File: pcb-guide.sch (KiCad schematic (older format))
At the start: 14 parts

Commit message: Tags added
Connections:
- net labels added: D+, D-
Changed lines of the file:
@@
 Wire Wire Line
 	2250 1400 2350 1400
+Text GLabel 1550 2400 0    50   Input ~ 0
+D+
+Text GLabel 1550 2500 0    50   Input ~ 0
+D-
 $EndSCHEMATC

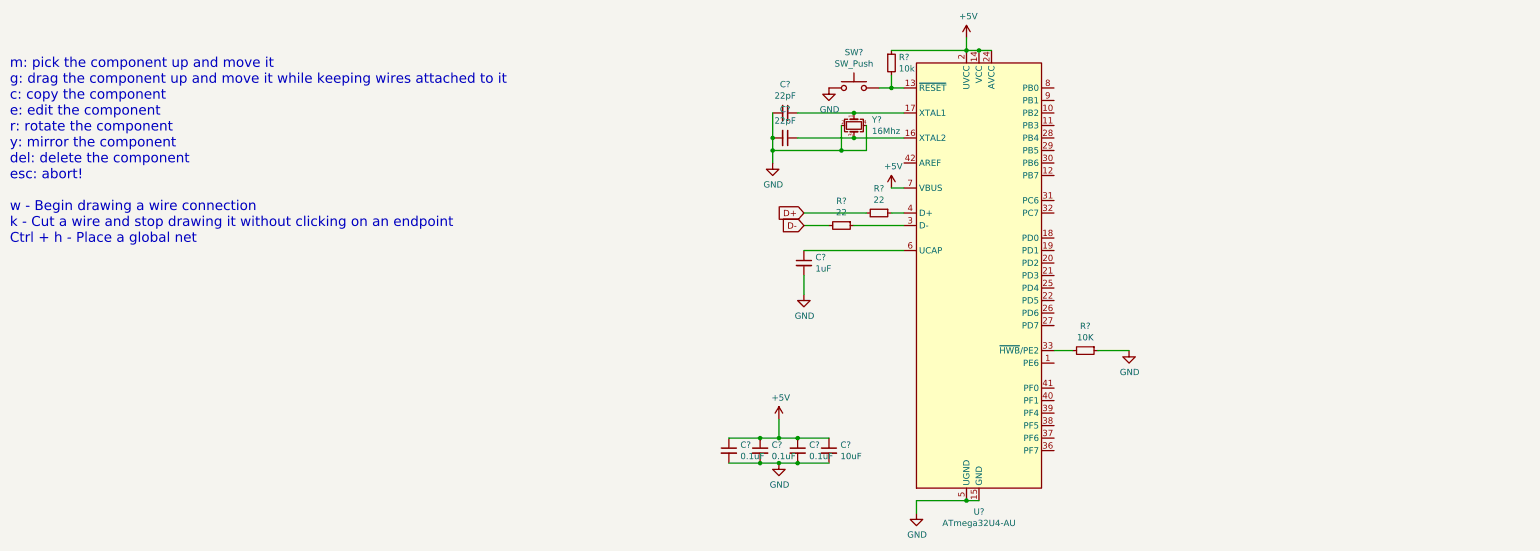
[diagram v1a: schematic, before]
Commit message: part4 finished mx_alps_hybrid not found in footpritn libraries
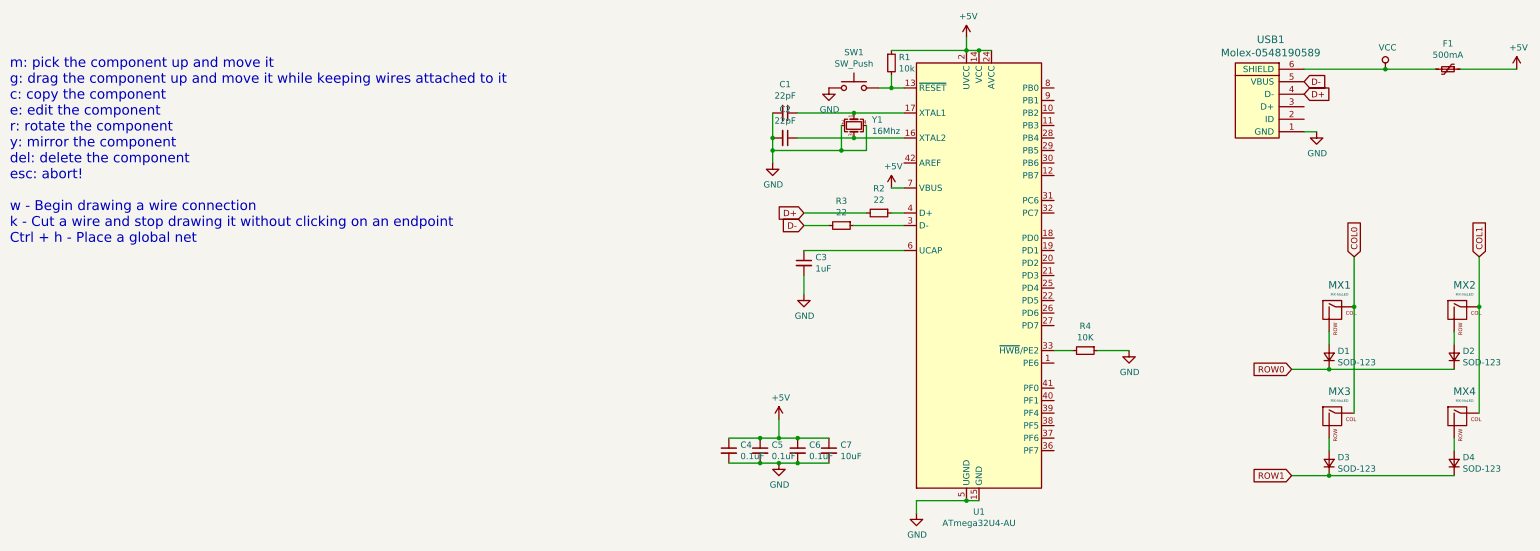
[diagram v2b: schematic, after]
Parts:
- added D1, D2, D3, D4: SOD-123, Diode_SMD:D_SOD-123, symbol Device:D_Small
- added F1: 500mA, Fuse:Fuse_1206_3216Metric, symbol Device:Polyfuse_Small
- added MX1, MX2, MX3, MX4: MX-NoLED, symbol MX_Alps_Hybrid:MX-NoLED
- added USB1: Molex-0548190589, random-keyboard-parts:Molex-0548190589, symbol random-keyboard-parts:Molex-0548190589
- C1, C2, C3, C4, C5, C6, C7: renamed from C?; footprint (none) -> Capacitor_SMD:C_0805_2012Metric
- R1, R2, R3, R4: renamed from R?; footprint (none) -> Resistor_SMD:R_0805_2012Metric
- SW1: renamed from SW?; footprint (none) -> random-keyboard-parts:SKQG-1155865
- Y1: renamed from Y?; footprint (none) -> Crystal:Crystal_SMD_3225-4Pin_3.2x2.5mm
- gave numbers to parts that had none: 1
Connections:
- net +5V: now also F1.1
- net D+: now also USB1.4 (D-)
- net D-: now also USB1.5 (VBUS)
- net GND: now also USB1.1 (GND)
- new net: D1.2 (A), MX1.2 (ROW)
- new net: D2.2 (A), MX2.2 (ROW)
- new net: D3.2 (A), MX3.2 (ROW)
- new net: D4.2 (A), MX4.2 (ROW)
- new net COL0: MX1.1 (COL), MX3.1 (COL)
- new net COL1: MX2.1 (COL), MX4.1 (COL)
- new net ROW0: D1.1 (K), D2.1 (K)
- new net ROW1: D3.1 (K), D4.1 (K)
- new net VCC: F1.2, USB1.6 (SHIELD)

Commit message: Error fixed with MX_ALPS_Hybrid
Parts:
- MX1, MX2, MX3, MX4: footprint (none) -> MX_Alps_Hybrid:MX-1U-NoLED
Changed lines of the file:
@@
 F 0 "MX1" H 5833 3423 60  0000 C CNN
 F 1 "MX-NoLED" H 5833 3349 20  0000 C CNN
-F 2 "" H 5175 3175 60  0001 C CNN
+F 2 "MX_Alps_Hybrid:MX-1U-NoLED" H 5175 3175 60  0001 C CNN
 F 3 "" H 5175 3175 60  0001 C CNN
 	1    5800 3200
@@
 F 0 "MX2" H 6833 3423 60  0000 C CNN
 F 1 "MX-NoLED" H 6833 3349 20  0000 C CNN
-F 2 "" H 6175 3175 60  0001 C CNN
+F 2 "MX_Alps_Hybrid:MX-1U-NoLED" H 6175 3175 60  0001 C CNN
 F 3 "" H 6175 3175 60  0001 C CNN
 	1    6800 3200
@@
 F 0 "MX3" H 5833 4273 60  0000 C CNN
 F 1 "MX-NoLED" H 5833 4199 20  0000 C CNN
-F 2 "" H 5175 4025 60  0001 C CNN
+F 2 "MX_Alps_Hybrid:MX-1U-NoLED" H 5175 4025 60  0001 C CNN
 F 3 "" H 5175 4025 60  0001 C CNN
 	1    5800 4050
@@
 F 0 "MX4" H 6833 4273 60  0000 C CNN
 F 1 "MX-NoLED" H 6833 4199 20  0000 C CNN
-F 2 "" H 6175 4025 60  0001 C CNN
+F 2 "MX_Alps_Hybrid:MX-1U-NoLED" H 6175 4025 60  0001 C CNN
 F 3 "" H 6175 4025 60  0001 C CNN
 	1    6800 4050

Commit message: part 5 almost finished
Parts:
- MX1, MX2, MX3, MX4: footprint MX_Alps_Hybrid:MX-1U-NoLED -> MX_Alps_Hybrid:MX-1U
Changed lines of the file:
@@
 F 0 "MX1" H 5833 3423 60  0000 C CNN
 F 1 "MX-NoLED" H 5833 3349 20  0000 C CNN
-F 2 "MX_Alps_Hybrid:MX-1U-NoLED" H 5175 3175 60  0001 C CNN
+F 2 "MX_Alps_Hybrid:MX-1U" H 5175 3175 60  0001 C CNN
 F 3 "" H 5175 3175 60  0001 C CNN
 	1    5800 3200
@@
 F 0 "MX2" H 6833 3423 60  0000 C CNN
 F 1 "MX-NoLED" H 6833 3349 20  0000 C CNN
-F 2 "MX_Alps_Hybrid:MX-1U-NoLED" H 6175 3175 60  0001 C CNN
+F 2 "MX_Alps_Hybrid:MX-1U" H 6175 3175 60  0001 C CNN
 F 3 "" H 6175 3175 60  0001 C CNN
 	1    6800 3200
@@
 F 0 "MX3" H 5833 4273 60  0000 C CNN
 F 1 "MX-NoLED" H 5833 4199 20  0000 C CNN
-F 2 "MX_Alps_Hybrid:MX-1U-NoLED" H 5175 4025 60  0001 C CNN
+F 2 "MX_Alps_Hybrid:MX-1U" H 5175 4025 60  0001 C CNN
 F 3 "" H 5175 4025 60  0001 C CNN
 	1    5800 4050
@@
 F 0 "MX4" H 6833 4273 60  0000 C CNN
 F 1 "MX-NoLED" H 6833 4199 20  0000 C CNN
-F 2 "MX_Alps_Hybrid:MX-1U-NoLED" H 6175 4025 60  0001 C CNN
+F 2 "MX_Alps_Hybrid:MX-1U" H 6175 4025 60  0001 C CNN
 F 3 "" H 6175 4025 60  0001 C CNN
 	1    6800 4050

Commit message: Finish
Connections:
- net COL0: now also U1.29 (PB5)
- net COL1: now also U1.28 (PB4)
- net ROW0: now also U1.27 (PD7)
- net ROW1: now also U1.30 (PB6)
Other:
- moved on the sheet: R4
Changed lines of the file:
@@
 L power:GND #PWR0103
 U 1 1 5FBEA79A
-P 4150 3500
-F 0 "#PWR0103" H 4150 3250 50  0001 C CNN
-F 1 "GND" H 4155 3327 50  0000 C CNN
-F 2 "" H 4150 3500 50  0001 C CNN
-F 3 "" H 4150 3500 50  0001 C CNN
-	1    4150 3500
+P 4400 3500
+F 0 "#PWR0103" H 4400 3250 50  0001 C CNN
+F 1 "GND" H 4405 3327 50  0000 C CNN
+F 2 "" H 4400 3500 50  0001 C CNN
+F 3 "" H 4400 3500 50  0001 C CNN
+	1    4400 3500
 	1    0    0    -1
 $EndComp
@@
 L Device:R_Small R4
 U 1 1 5FBEB9A0
-P 3800 3500
-F 0 "R4" V 3604 3500 50  0000 C CNN
-F 1 "10K" V 3695 3500 50  0000 C CNN
-F 2 "Resistor_SMD:R_0805_2012Metric" H 3800 3500 50  0001 C CNN
-F 3 "~" H 3800 3500 50  0001 C CNN
-	1    3800 3500
-	0    1    1    0
-$EndComp
-Wire Wire Line
-	3550 3500 3700 3500
-Wire Wire Line
-	3900 3500 4150 3500
+P 4050 3500
+F 0 "R4" V 3854 3500 50  0000 C CNN
+F 1 "10K" V 3945 3500 50  0000 C CNN
+F 2 "Resistor_SMD:R_0805_2012Metric" H 4050 3500 50  0001 C CNN
+F 3 "~" H 4050 3500 50  0001 C CNN
+	1    4050 3500
+	0    1    1    0
+$EndComp
+Wire Wire Line
+	4150 3500 4400 3500
 $Comp
 L Device:R_Small R2
@@
 Text GLabel 6950 2750 1    50   Input ~ 0
 COL1
+Text GLabel 3550 1800 2    50   Input ~ 0
+COL1
+Text GLabel 3550 1900 2    50   Input ~ 0
+COL0
+Text GLabel 3550 2000 2    50   Input ~ 0
+ROW1
+Text GLabel 3550 3300 2    50   Input ~ 0
+ROW0
+Wire Wire Line
+	3950 3500 3550 3500
 $EndSCHEMATC

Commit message: PCB finished
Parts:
- MX1, MX2, MX3, MX4: footprint MX_Alps_Hybrid:MX-1U -> MX_Only:MXOnly-1U
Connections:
- net D+: now also USB1.3 (D+); no longer USB1.4 (D-)
- net D-: now also USB1.4 (D-); no longer USB1.5 (VBUS)
- net VCC: now also USB1.5 (VBUS); no longer USB1.6 (SHIELD)
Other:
- moved on the sheet: F1, USB1
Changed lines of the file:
@@
 $EndComp
-Wire Wire Line
-	2950 4700 2850 4700
 Wire Wire Line
 	2850 4700 2450 4700
 Wire Wire Line
 	2450 4700 2450 4800
-Connection ~ 2850 4700
 $Comp
 L power:GND #PWR0103
@@
 L random-keyboard-parts:Molex-0548190589 USB1
 U 1 1 5FC20C0B
-P 5250 1550
-F 0 "USB1" V 5787 1517 60  0000 C CNN
-F 1 "Molex-0548190589" V 5681 1517 60  0000 C CNN
-F 2 "random-keyboard-parts:Molex-0548190589" H 5250 1550 60  0001 C CNN
-F 3 "" H 5250 1550 60  0001 C CNN
-	1    5250 1550
+P 5100 1550
+F 0 "USB1" V 5637 1517 60  0000 C CNN
+F 1 "Molex-0548190589" V 5531 1517 60  0000 C CNN
+F 2 "random-keyboard-parts:Molex-0548190589" H 5100 1550 60  0001 C CNN
+F 3 "" H 5100 1550 60  0001 C CNN
+	1    5100 1550
 	0    -1   -1   0
 $EndComp
-$Comp
-L power:VCC #PWR0110
-U 1 1 5FC21D9D
-P 6200 1250
-F 0 "#PWR0110" H 6200 1100 50  0001 C CNN
-F 1 "VCC" H 6217 1423 50  0000 C CNN
-F 2 "" H 6200 1250 50  0001 C CNN
-F 3 "" H 6200 1250 50  0001 C CNN
-	1    6200 1250
-	1    0    0    -1
-$EndComp
-$Comp
-L Device:Polyfuse_Small F1
-U 1 1 5FC22CD6
-P 6700 1250
-F 0 "F1" V 6495 1250 50  0000 C CNN
-F 1 "500mA" V 6586 1250 50  0000 C CNN
-F 2 "Fuse:Fuse_1206_3216Metric" H 6750 1050 50  0001 L CNN
-F 3 "~" H 6700 1250 50  0001 C CNN
-	1    6700 1250
-	0    1    1    0
-$EndComp
-$Comp
-L power:+5V #PWR0111
-U 1 1 5FC23944
-P 7250 1250
-F 0 "#PWR0111" H 7250 1100 50  0001 C CNN
-F 1 "+5V" H 7265 1423 50  0000 C CNN
-F 2 "" H 7250 1250 50  0001 C CNN
-F 3 "" H 7250 1250 50  0001 C CNN
-	1    7250 1250
-	1    0    0    -1
-$EndComp
-Wire Wire Line
-	5550 1250 6200 1250
-Wire Wire Line
-	6600 1250 6200 1250
-Connection ~ 6200 1250
-Wire Wire Line
-	6800 1250 7250 1250
-Text GLabel 5550 1450 2    50   Input ~ 0
+Text GLabel 5400 1550 2    50   Input ~ 0
 D+
-Text GLabel 5550 1350 2    50   Input ~ 0
+Text GLabel 5400 1450 2    50   Input ~ 0
 D-
 $Comp
 L power:GND #PWR0112
 U 1 1 5FC2A78A
-P 5650 1750
-F 0 "#PWR0112" H 5650 1500 50  0001 C CNN
-F 1 "GND" H 5655 1577 50  0000 C CNN
-F 2 "" H 5650 1750 50  0001 C CNN
-F 3 "" H 5650 1750 50  0001 C CNN
-	1    5650 1750
-	1    0    0    -1
-$EndComp
-Wire Wire Line
-	5550 1750 5650 1750
+P 5500 1750
+F 0 "#PWR0112" H 5500 1500 50  0001 C CNN
+F 1 "GND" H 5505 1577 50  0000 C CNN
+F 2 "" H 5500 1750 50  0001 C CNN
+F 3 "" H 5500 1750 50  0001 C CNN
+	1    5500 1750
+	1    0    0    -1
+$EndComp
+Wire Wire Line
+	5400 1750 5500 1750
 $Comp
 L MX_Alps_Hybrid:MX-NoLED MX1
@@
 F 0 "MX1" H 5833 3423 60  0000 C CNN
 F 1 "MX-NoLED" H 5833 3349 20  0000 C CNN
-F 2 "MX_Alps_Hybrid:MX-1U" H 5175 3175 60  0001 C CNN
+F 2 "MX_Only:MXOnly-1U" H 5175 3175 60  0001 C CNN
 F 3 "" H 5175 3175 60  0001 C CNN
 	1    5800 3200
@@
 F 0 "MX2" H 6833 3423 60  0000 C CNN
 F 1 "MX-NoLED" H 6833 3349 20  0000 C CNN
-F 2 "MX_Alps_Hybrid:MX-1U" H 6175 3175 60  0001 C CNN
+F 2 "MX_Only:MXOnly-1U" H 6175 3175 60  0001 C CNN
 F 3 "" H 6175 3175 60  0001 C CNN
 	1    6800 3200
@@
 F 0 "MX3" H 5833 4273 60  0000 C CNN
 F 1 "MX-NoLED" H 5833 4199 20  0000 C CNN
-F 2 "MX_Alps_Hybrid:MX-1U" H 5175 4025 60  0001 C CNN
+F 2 "MX_Only:MXOnly-1U" H 5175 4025 60  0001 C CNN
 F 3 "" H 5175 4025 60  0001 C CNN
 	1    5800 4050
@@
 F 0 "MX4" H 6833 4273 60  0000 C CNN
 F 1 "MX-NoLED" H 6833 4199 20  0000 C CNN
-F 2 "MX_Alps_Hybrid:MX-1U" H 6175 4025 60  0001 C CNN
+F 2 "MX_Only:MXOnly-1U" H 6175 4025 60  0001 C CNN
 F 3 "" H 6175 4025 60  0001 C CNN
 	1    6800 4050
@@
 Wire Wire Line
 	3950 3500 3550 3500
+Wire Wire Line
+	6650 1350 7100 1350
+Connection ~ 6050 1350
+Wire Wire Line
+	6450 1350 6050 1350
+Wire Wire Line
+	5400 1350 6050 1350
+$Comp
+L power:+5V #PWR0111
+U 1 1 5FC23944
+P 7100 1350
+F 0 "#PWR0111" H 7100 1200 50  0001 C CNN
+F 1 "+5V" H 7115 1523 50  0000 C CNN
+F 2 "" H 7100 1350 50  0001 C CNN
+F 3 "" H 7100 1350 50  0001 C CNN
+	1    7100 1350
+	1    0    0    -1
+$EndComp
+$Comp
+L Device:Polyfuse_Small F1
+U 1 1 5FC22CD6
+P 6550 1350
+F 0 "F1" V 6345 1350 50  0000 C CNN
+F 1 "500mA" V 6436 1350 50  0000 C CNN
+F 2 "Fuse:Fuse_1206_3216Metric" H 6600 1150 50  0001 L CNN
+F 3 "~" H 6550 1350 50  0001 C CNN
+	1    6550 1350
+	0    1    1    0
+$EndComp
+$Comp
+L power:VCC #PWR0110
+U 1 1 5FC21D9D
+P 6050 1350
+F 0 "#PWR0110" H 6050 1200 50  0001 C CNN
+F 1 "VCC" H 6067 1523 50  0000 C CNN
+F 2 "" H 6050 1350 50  0001 C CNN
+F 3 "" H 6050 1350 50  0001 C CNN
+	1    6050 1350
+	1    0    0    -1
+$EndComp
+Connection ~ 2850 4700
+Wire Wire Line
+	2950 4700 2850 4700
 $EndSCHEMATC
